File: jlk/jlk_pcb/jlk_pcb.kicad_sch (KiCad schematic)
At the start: 44 parts, among them SW0 SWITCH_PUSH, SW1 SWITCH_PUSH, SW10 SWITCH_PUSH, SW11 SWITCH_PUSH, SW12 SWITCH_PUSH, SW13 SWITCH_PUSH, SW14 SWITCH_PUSH, SW15 SWITCH_PUSH, SW16 SWITCH_PUSH, SW17 SWITCH_PUSH, SW18 SWITCH_PUSH, SW19 SWITCH_PUSH, SW2 SWITCH_PUSH, SW20 SWITCH_PUSH, SW21 SWITCH_PUSH, SW22 SWITCH_PUSH, SW23 SWITCH_PUSH, SW24 SWITCH_PUSH, SW25 SWITCH_PUSH, SW26 SWITCH_PUSH, SW27 SWITCH_PUSH, SW28 SWITCH_PUSH, SW29 SWITCH_PUSH, SW3 SWITCH_PUSH, SW30 SWITCH_PUSH, SW31 SWITCH_PUSH, SW32 SWITCH_PUSH, SW33 SWITCH_PUSH, SW4 SWITCH_PUSH, SW5 SWITCH_PUSH, SW6 SWITCH_PUSH, SW7 SWITCH_PUSH, SW8 SWITCH_PUSH, SW9 SWITCH_PUSH, U0 ARDUINO_PRO_MICRO

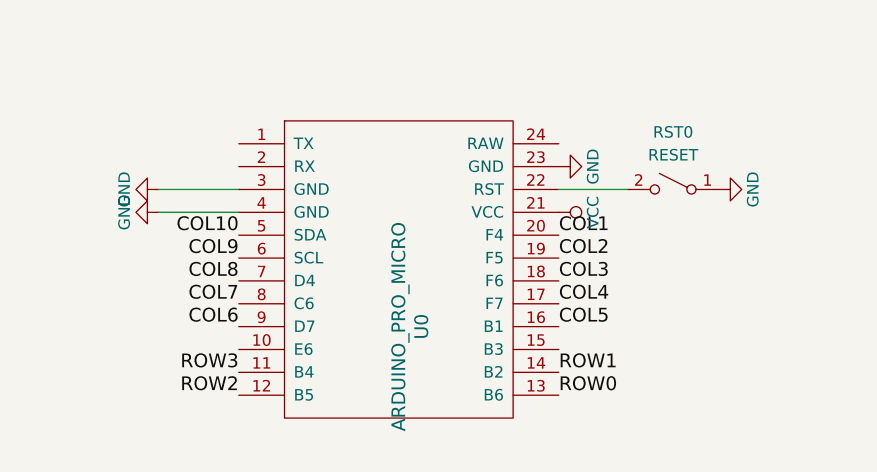
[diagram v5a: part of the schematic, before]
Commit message: Changed jlk for mounting promicro under the pcb.
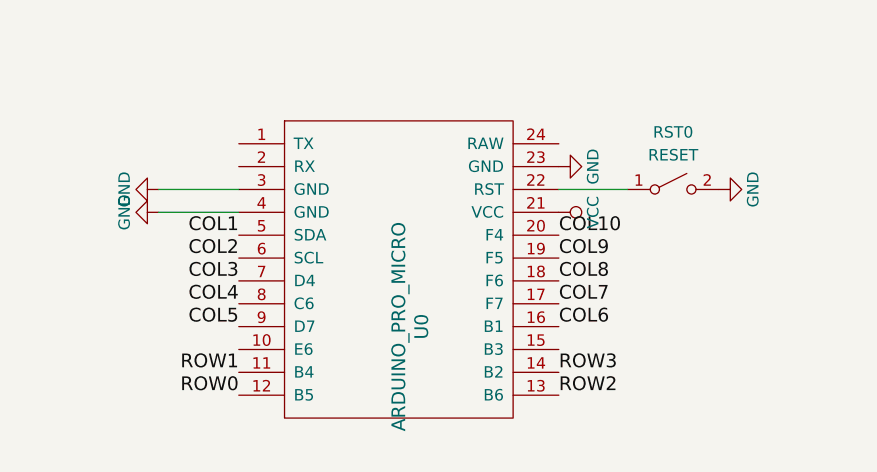
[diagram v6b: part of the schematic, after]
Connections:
- net COL1: now also U0.5 (SDA); no longer U0.20 (F4)
- net COL10: now also U0.20 (F4); no longer U0.5 (SDA)
- net COL2: now also U0.6 (SCL); no longer U0.19 (F5)
- net COL3: now also U0.7 (D4); no longer U0.18 (F6)
- net COL4: now also U0.8 (C6); no longer U0.17 (F7)
- net COL5: now also U0.9 (D7); no longer U0.16 (B1)
- net COL6: now also U0.16 (B1); no longer U0.9 (D7)
- net COL7: now also U0.17 (F7); no longer U0.8 (C6)
- net COL8: now also U0.18 (F6); no longer U0.7 (D4)
- net COL9: now also U0.19 (F5); no longer U0.6 (SCL)
- net GND: now also RST0.2 (B); no longer RST0.1 (A)
- net ROW0: now also U0.12 (B5); no longer U0.13 (B6)
- net ROW1: now also U0.11 (B4); no longer U0.14 (B2)
- net ROW2: now also U0.13 (B6); no longer U0.12 (B5)
- net ROW3: now also U0.14 (B2); no longer U0.11 (B4)
- net at U0.22 (RST): now also RST0.1 (A); no longer RST0.2 (B)
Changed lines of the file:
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@@
     (stroke (width 0) (type default))
   )
-  (label "COL5" (at 198.12 165.1 0) (fields_autoplaced)
+  (label "COL5" (at 162.56 165.1 180) (fields_autoplaced)
+    (effects (font (size 1.524 1.524)) (justify right bottom))
+  )
+  (label "COL2" (at 77.47 116.84 270) (fields_autoplaced)
+    (effects (font (size 1.524 1.524)) (justify right bottom))
+  )
+  (label "COL1" (at 162.56 154.94 180) (fields_autoplaced)
+    (effects (font (size 1.524 1.524)) (justify right bottom))
+  )
+  (label "COL8" (at 198.12 160.02 0) (fields_autoplaced)
     (effects (font (size 1.524 1.524)) (justify left bottom))
   )
-  (label "COL2" (at 77.47 116.84 270) (fields_autoplaced)
-    (effects (font (size 1.524 1.524)) (justify right bottom))
-  )
-  (label "COL1" (at 198.12 154.94 0) (fields_autoplaced)
+  (label "COL10" (at 294.64 116.84 270) (fields_autoplaced)
+    (effects (font (size 1.524 1.524)) (justify right bottom))
+  )
+  (label "ROW2" (at 21.59 71.12 180) (fields_autoplaced)
+    (effects (font (size 1.524 1.524)) (justify right bottom))
+  )
+  (label "COL6" (at 198.12 165.1 0) (fields_autoplaced)
     (effects (font (size 1.524 1.524)) (justify left bottom))
   )
-  (label "COL8" (at 162.56 160.02 180) (fields_autoplaced)
-    (effects (font (size 1.524 1.524)) (justify right bottom))
-  )
-  (label "COL10" (at 294.64 116.84 270) (fields_autoplaced)
-    (effects (font (size 1.524 1.524)) (justify right bottom))
-  )
-  (label "ROW2" (at 21.59 71.12 180) (fields_autoplaced)
-    (effects (font (size 1.524 1.524)) (justify right bottom))
-  )
-  (label "COL6" (at 162.56 165.1 180) (fields_autoplaced)
-    (effects (font (size 1.524 1.524)) (justify right bottom))
-  )
   (label "COL8" (at 246.38 116.84 270) (fields_autoplaced)
     (effects (font (size 1.524 1.524)) (justify right bottom))
   )
-  (label "COL3" (at 198.12 160.02 0) (fields_autoplaced)
+  (label "COL3" (at 162.56 160.02 180) (fields_autoplaced)
+    (effects (font (size 1.524 1.524)) (justify right bottom))
+  )
+  (label "ROW0" (at 162.56 172.72 180) (fields_autoplaced)
+    (effects (font (size 1.524 1.524)) (justify right bottom))
+  )
+  (label "COL1" (at 53.34 116.84 270) (fields_autoplaced)
+    (effects (font (size 1.524 1.524)) (justify right bottom))
+  )
+  (label "COL9" (at 270.51 116.84 270) (fields_autoplaced)
+    (effects (font (size 1.524 1.524)) (justify right bottom))
+  )
+  (label "COL7" (at 198.12 162.56 0) (fields_autoplaced)
     (effects (font (size 1.524 1.524)) (justify left bottom))
   )
-  (label "ROW0" (at 198.12 172.72 0) (fields_autoplaced)
+  (label "COL6" (at 198.12 116.84 270) (fields_autoplaced)
+    (effects (font (size 1.524 1.524)) (justify right bottom))
+  )
+  (label "COL3" (at 101.6 116.84 270) (fields_autoplaced)
+    (effects (font (size 1.524 1.524)) (justify right bottom))
+  )
+  (label "COL4" (at 162.56 162.56 180) (fields_autoplaced)
+    (effects (font (size 1.524 1.524)) (justify right bottom))
+  )
+  (label "COL10" (at 198.12 154.94 0) (fields_autoplaced)
     (effects (font (size 1.524 1.524)) (justify left bottom))
   )
-  (label "COL1" (at 53.34 116.84 270) (fields_autoplaced)
-    (effects (font (size 1.524 1.524)) (justify right bottom))
-  )
-  (label "COL9" (at 270.51 116.84 270) (fields_autoplaced)
-    (effects (font (size 1.524 1.524)) (justify right bottom))
-  )
-  (label "COL7" (at 162.56 162.56 180) (fields_autoplaced)
-    (effects (font (size 1.524 1.524)) (justify right bottom))
-  )
-  (label "COL6" (at 198.12 116.84 270) (fields_autoplaced)
-    (effects (font (size 1.524 1.524)) (justify right bottom))
-  )
-  (label "COL3" (at 101.6 116.84 270) (fields_autoplaced)
-    (effects (font (size 1.524 1.524)) (justify right bottom))
-  )
-  (label "COL4" (at 198.12 162.56 0) (fields_autoplaced)
+  (label "ROW1" (at 162.56 170.18 180) (fields_autoplaced)
+    (effects (font (size 1.524 1.524)) (justify right bottom))
+  )
+  (label "ROW3" (at 198.12 170.18 0) (fields_autoplaced)
     (effects (font (size 1.524 1.524)) (justify left bottom))
   )
-  (label "COL10" (at 162.56 154.94 180) (fields_autoplaced)
-    (effects (font (size 1.524 1.524)) (justify right bottom))
-  )
-  (label "ROW1" (at 198.12 170.18 0) (fields_autoplaced)
+  (label "COL9" (at 198.12 157.48 0) (fields_autoplaced)
     (effects (font (size 1.524 1.524)) (justify left bottom))
   )
-  (label "ROW3" (at 162.56 170.18 180) (fields_autoplaced)
-    (effects (font (size 1.524 1.524)) (justify right bottom))
-  )
-  (label "COL9" (at 162.56 157.48 180) (fields_autoplaced)
-    (effects (font (size 1.524 1.524)) (justify right bottom))
-  )
   (label "ROW3" (at 21.59 53.34 180) (fields_autoplaced)
     (effects (font (size 1.524 1.524)) (justify right bottom))
@@
     (effects (font (size 1.524 1.524)) (justify right bottom))
   )
-  (label "COL2" (at 198.12 157.48 0) (fields_autoplaced)
+  (label "COL2" (at 162.56 157.48 180) (fields_autoplaced)
+    (effects (font (size 1.524 1.524)) (justify right bottom))
+  )
+  (label "ROW2" (at 198.12 172.72 0) (fields_autoplaced)
     (effects (font (size 1.524 1.524)) (justify left bottom))
-  )
-  (label "ROW2" (at 162.56 172.72 180) (fields_autoplaced)
-    (effects (font (size 1.524 1.524)) (justify right bottom))
   )
   (label "ROW1" (at 21.59 88.9 180) (fields_autoplaced)
@@
     )
   )
-  (symbol (lib_id "Switch:SW_SPST") (at 210.82 149.86 0) (mirror y) (unit 1)
+  (symbol (lib_id "Switch:SW_SPST") (at 210.82 149.86 0) (unit 1)
     (in_bom yes) (on_board yes) (dnp no)
     (property "Reference" "RST0" (at 210.82 143.51 0)

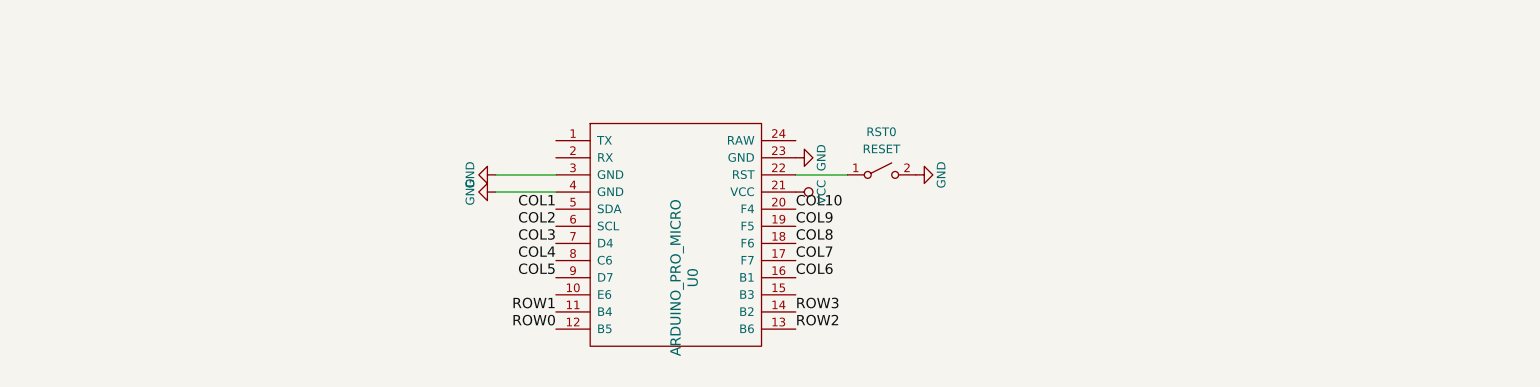
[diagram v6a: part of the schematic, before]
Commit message: Switched jlk to use nice!nano.
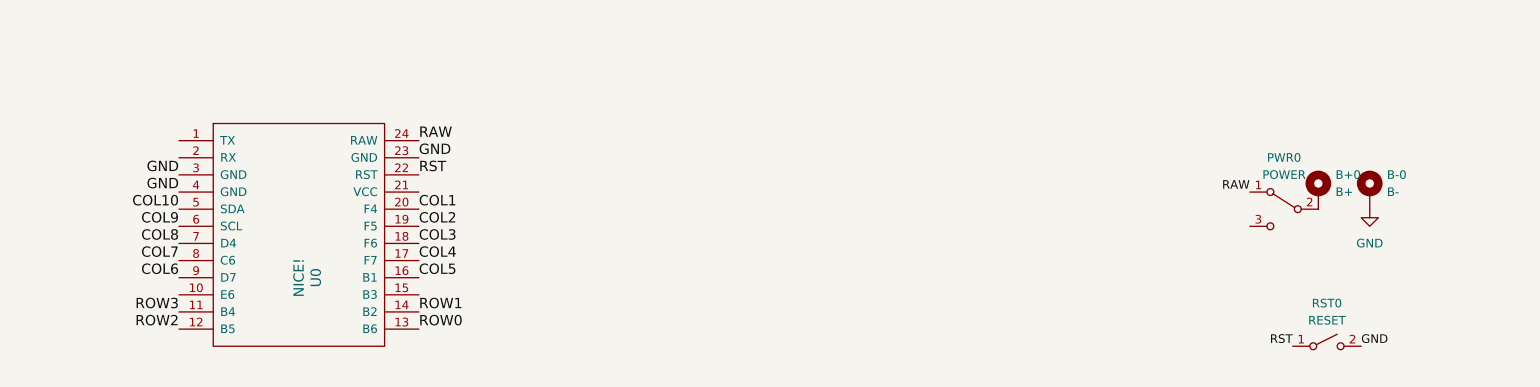
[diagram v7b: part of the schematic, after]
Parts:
- added B+0: B+, Connector_Pin:Pin_D0.9mm_L10.0mm_W2.4mm_FlatFork, symbol Mechanical:MountingHole_Pad
- added B-0: B-, Connector_Pin:Pin_D0.9mm_L10.0mm_W2.4mm_FlatFork, symbol Mechanical:MountingHole_Pad
- added PWR0: POWER, footprints:AYZ0102AGRLC, symbol Switch:SW_SPDT
- U0: value ARDUINO_PRO_MICRO -> NICE!; footprint footprints:ARDUINO_PRO_MICRO -> footprints:nice!nano
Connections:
- net COL1: now also U0.20 (F4); no longer U0.5 (SDA)
- net COL10: now also U0.5 (SDA); no longer U0.20 (F4)
- net COL2: now also U0.19 (F5); no longer U0.6 (SCL)
- net COL3: now also U0.18 (F6); no longer U0.7 (D4)
- net COL4: now also U0.17 (F7); no longer U0.8 (C6)
- net COL5: now also U0.16 (B1); no longer U0.9 (D7)
- net COL6: now also U0.9 (D7); no longer U0.16 (B1)
- net COL7: now also U0.8 (C6); no longer U0.17 (F7)
- net COL8: now also U0.7 (D4); no longer U0.18 (F6)
- net COL9: now also U0.6 (SCL); no longer U0.19 (F5)
- net GND: now also B-0.1
- net ROW0: now also U0.13 (B6); no longer U0.12 (B5)
- net ROW1: now also U0.14 (B2); no longer U0.11 (B4)
- net ROW2: now also U0.12 (B5); no longer U0.13 (B6)
- net ROW3: now also U0.11 (B4); no longer U0.14 (B2)
- net RST: now reaches RST0.1 (A), U0.22 (RST)
- net RAW: now reaches U0.24 (RAW)
- net RAW: now also PWR0.1 (A)
- net VCC: no longer names the net of U0.21 (VCC)
- new net: B+0.1, PWR0.2 (B)
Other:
- moved on the sheet: RST0, U0

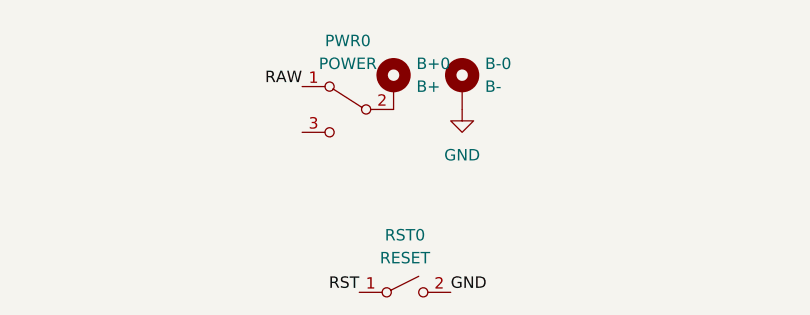
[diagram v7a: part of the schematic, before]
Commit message: Changed the reset and power switches for kfs and jlk.
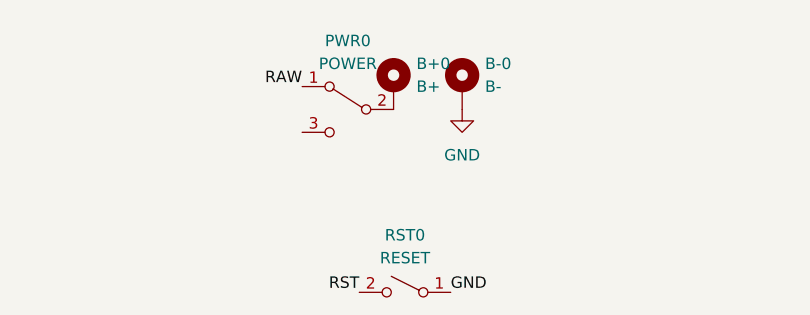
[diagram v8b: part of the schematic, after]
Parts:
- PWR0: footprint footprints:AYZ0102AGRLC -> footprints:power_switch
- RST0: footprint footprints:reset_button_1 -> footprints:reset_button_2
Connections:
- net GND: now also RST0.1 (A); no longer RST0.2 (B)
- net RST: now also RST0.2 (B); no longer RST0.1 (A)
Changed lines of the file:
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@@
       (effects (font (size 1.27 1.27)))
     )
-    (property "Footprint" "footprints:AYZ0102AGRLC" (at 270.51 154.94 0)
+    (property "Footprint" "footprints:power_switch" (at 270.51 154.94 0)
       (effects (font (size 1.27 1.27)) hide)
     )
@@
     )
   )
-  (symbol (lib_id "Switch:SW_SPST") (at 276.86 175.26 0) (unit 1)
+  (symbol (lib_id "Switch:SW_SPST") (at 276.86 175.26 0) (mirror y) (unit 1)
     (in_bom yes) (on_board yes) (dnp no)
     (property "Reference" "RST0" (at 276.86 168.91 0)
@@
       (effects (font (size 1.27 1.27)))
     )
-    (property "Footprint" "footprints:reset_button_1" (at 276.86 175.26 0)
+    (property "Footprint" "footprints:reset_button_2" (at 276.86 175.26 0)
       (effects (font (size 1.27 1.27)) hide)
     )
